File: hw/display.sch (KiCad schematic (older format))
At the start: 22 parts, among them J1 AMPSEAL_8_POS_776275-1, J101 HEADER_MOLEX_54104-4031, J4 HEADER_MOLEX_52207-0433, U1 MCP2551_SOIC8, U2 ALLIANCE_AS4C4M16SA_TSOP_II, U3 WINDBOND_W25Q32FV_SOIC8_W, U6 MOSFET-N_2N7002W, X101 XTAL_ABS25-32.768KHZ-T, X3 BUZZER_PKM13EPYH4002-B0

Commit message: still implementing treeview, not ready
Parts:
- removed U6: MOSFET-N_2N7002W, usevolt:SOT323, symbol MOSFET-N_2N7002W-RESCUE-display
- added C101: 100nF, kemet:0603, symbol 100nF
- added D101: DIODE_RS07J-GS18, usevolt:DO219AB, symbol DIODE_RS07J-GS18
- added L101: INDUCTOR_SDR1005-101KL, usevolt:INDUCTOR_BOURNS_10X13X5MM, symbol INDUCTOR_SDR1005-101KL
- added R101: R_0.33OHM, usevolt:0603, symbol R_0.33OHM
- added U101: MOSFET-N_2N7002W, usevolt:SOT323, symbol MOSFET-N_2N7002W
- added U102: AL8805W5-7_LED_DRIVER, usevolt:SOT-25, symbol AL8805W5-7_LED_DRIVER
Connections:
- wire segments 272 -> 287
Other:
- moved on the sheet: J101, X3

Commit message: hw 1.5.0 ordered
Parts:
- U1: symbol MCP2551_SOIC8 -> MCP2551_SOIC8-RESCUE-display
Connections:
- net +5V: now also U1.P$3 (VDD); no longer U1.8 (RS/GND)
- net CANH: now also U1.P$7 (CANH)
- net CANL: now also U1.P$6 (CANL)
- net GND: now also U1.P$2 (VSS), U1.P$8 (RS); no longer U1.5 (VREF)
- net lpc1785_sheet/CAN_RXD: now also U1.P$4 (RXD)
- net lpc1785_sheet/CAN_TXD: now also U1.P$1 (TXD)
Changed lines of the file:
@@
 CANL
 $Comp
-L MCP2551_SOIC8 U1
+L MCP2551_SOIC8-RESCUE-display U1
 U 1 1 57BD7966
 P 2900 3300

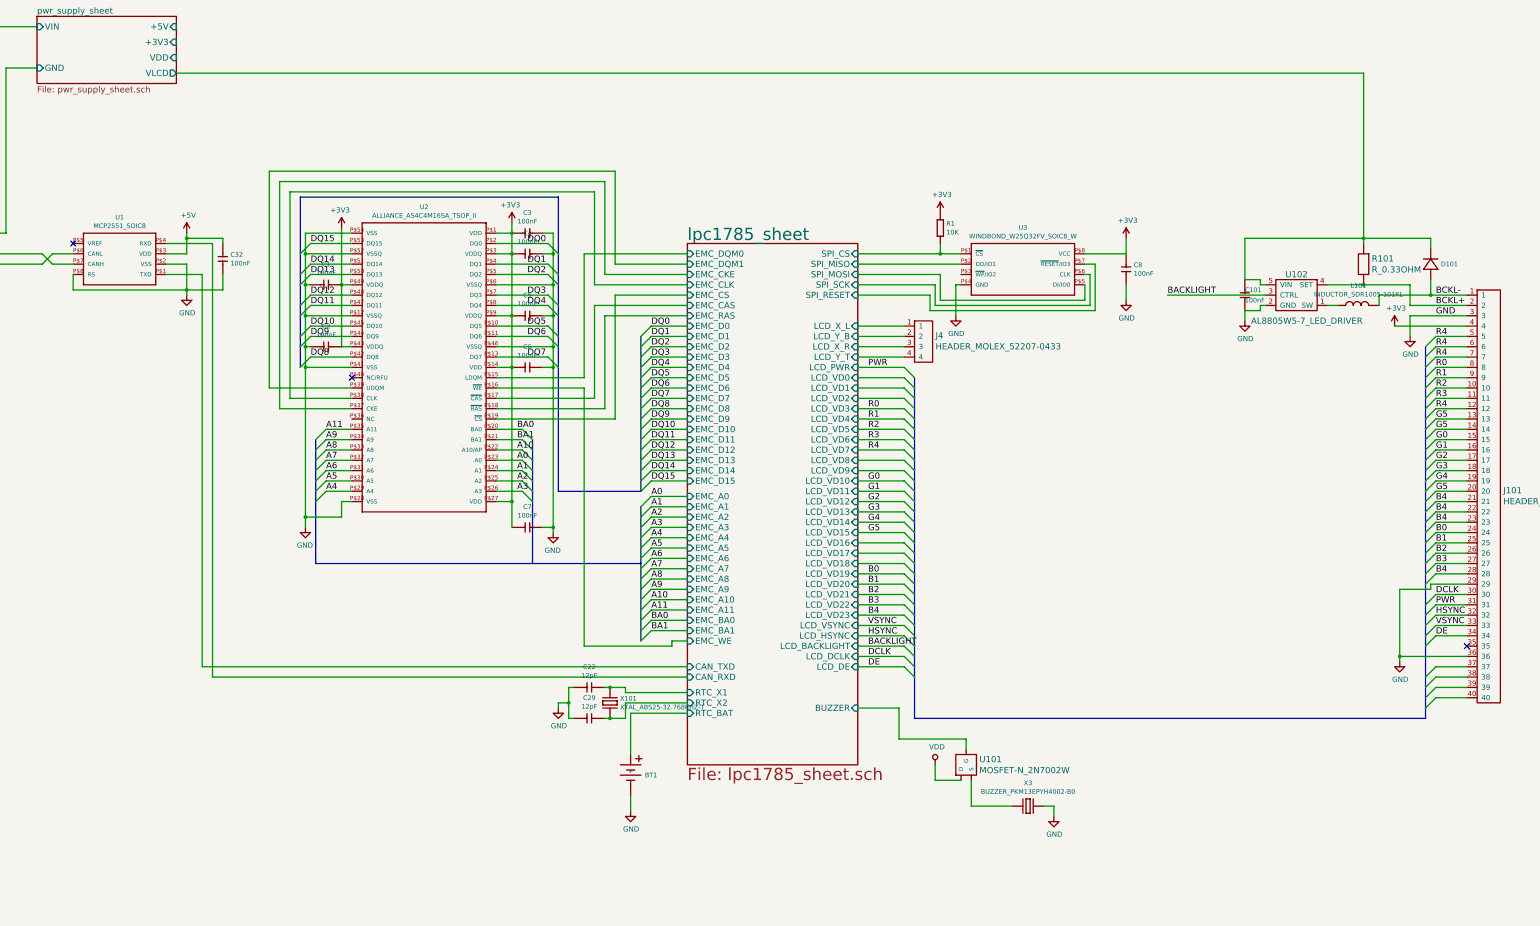
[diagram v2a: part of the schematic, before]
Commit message: hw version 1.6.0
* LCD backlight remains off while booting
* BUZZER amplifying MOSFET circuit changed to low side driving
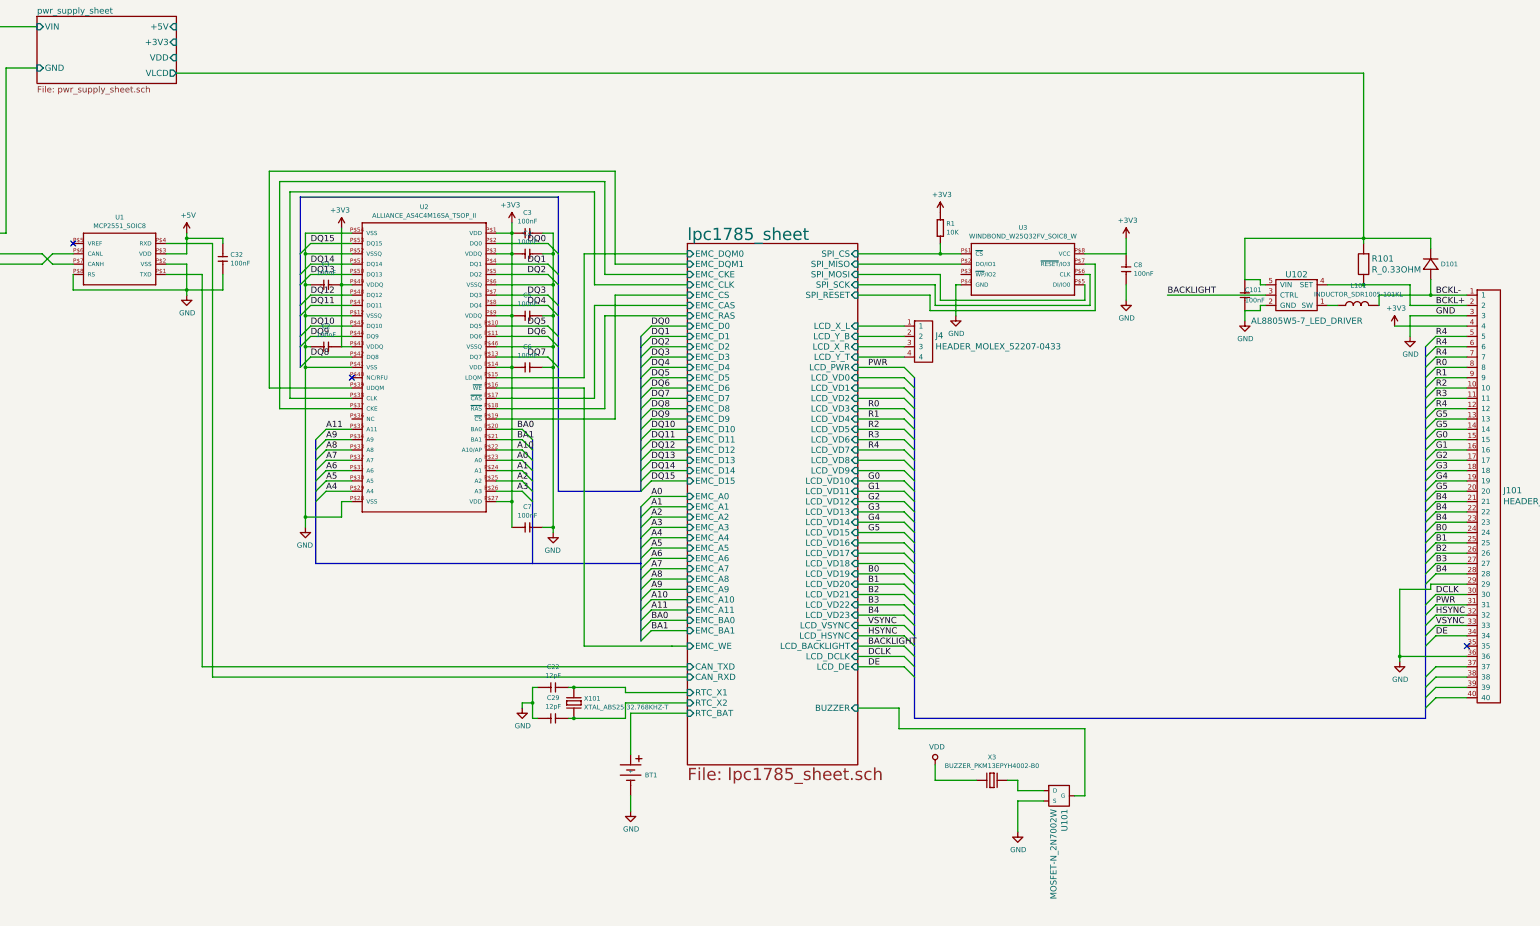
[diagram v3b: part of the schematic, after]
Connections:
- net GND: now also U101.R (S); no longer X3.2 (P$2)
- net VDD: now also X3.1 (P$1); no longer U101.M (D)
- new net: U101.M (D), X3.2 (P$2)
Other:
- moved on the sheet: C22, C29, U101, X101, X3

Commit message: implementing a multilinguality
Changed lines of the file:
@@
 	14750 3600 15600 3600
 Wire Bus Line
-	10250 7700 15200 7700
-Wire Bus Line
-	10250 4400 10250 7700
+	15200 7700 10250 7700
+Wire Bus Line
+	10250 7700 10250 4400
 Wire Wire Line
 	15300 7500 15600 7500
@@
 	7600 4000 7600 5500
 Wire Bus Line
-	6800 5500 7600 5500
-Wire Bus Line
-	6800 2650 6800 5500
+	7600 5500 6800 5500
+Wire Bus Line
+	6800 5500 6800 2650
 Wire Bus Line
 	6800 2650 4300 2650
@@
 Wire Wire Line
 	14600 1450 3100 1450
-$Comp
-L INDUCTOR_SDR1005-101KL L101
-U 1 1 58F7C6AA
-P 14550 3700
-F 0 "L101" H 14550 3891 45  0000 C CNN
-F 1 "INDUCTOR_SDR1005-101KL" H 14550 3807 45  0000 C CNN
-F 2 "usevolt:INDUCTOR_BOURNS_10X13X5MM" H 14580 3850 20  0001 C CNN
-F 3 "http://www.farnell.com/datasheets/1695384.pdf?_ga=1.223340891.1948984246.1460023966" H 14450 3640 60  0001 C CNN
-F 4 "1828057" H 14850 4040 60  0001 C CNN "1st Source Part Number"
-F 5 "BOURNS" H 14550 3740 60  0001 C CNN "Manufacturer"
-F 6 "Digi-Key" H 14950 4140 60  0001 C CNN "2nd Source"
-F 7 "Farnell" H 14750 3940 60  0001 C CNN "1st Source"
-F 8 "SDR1005-101KL" H 14650 3840 60  0001 C CNN "Manufacturer Part Number"
-F 9 "SDR1005-101KLCT-ND" H 15050 4240 60  0001 C CNN "2nd Source Part Number"
-	1    14550 3700
-	1    0    0    -1
-$EndComp
 Wire Wire Line
 	10450 8300 10850 8300
@@
 Wire Wire Line
 	10500 3650 11900 3650
+$Comp
+L INDUCTOR_SDR1005-101KL L101
+U 1 1 58F7C6AA
+P 14550 3700
+F 0 "L101" H 14550 3891 45  0000 C CNN
+F 1 "INDUCTOR_SDR1005-101KL" H 14550 3807 45  0000 C CNN
+F 2 "usevolt:INDUCTOR_BOURNS_10X13X5MM" H 14580 3850 20  0001 C CNN
+F 3 "http://www.farnell.com/datasheets/1695384.pdf?_ga=1.223340891.1948984246.1460023966" H 14450 3640 60  0001 C CNN
+F 4 "1828057" H 14850 4040 60  0001 C CNN "1st Source Part Number"
+F 5 "BOURNS" H 14550 3740 60  0001 C CNN "Manufacturer"
+F 6 "Digi-Key" H 14950 4140 60  0001 C CNN "2nd Source"
+F 7 "Farnell" H 14750 3940 60  0001 C CNN "1st Source"
+F 8 "SDR1005-101KL" H 14650 3840 60  0001 C CNN "Manufacturer Part Number"
+F 9 "SDR1005-101KLCT-ND" H 15050 4240 60  0001 C CNN "2nd Source Part Number"
+	1    14550 3700
+	1    0    0    -1
+$EndComp
 $EndSCHEMATC

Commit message: porting uv0a_hds pcb to uw_display
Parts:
- removed BT1: BATTERY_HOLDER_CH7410-2032LFSMD, usevolt:usevolt-BATTERY_HOLDER_CH7410-2032LF, symbol BATTERY_HOLDER_CH7410-2032LFSMD
- removed C1, C2, C3, C32, C4, C5, C6, C7, C8: 100nF, kemet:Kemet-CAPC1608X85N, symbol 100nF
- removed C22, C29: 12pF, kemet:Kemet-CAPC1608X85N, symbol 12pF
- removed D101: DIODE_RS07J-GS18, usevolt:DO219AB, symbol DIODE_RS07J-GS18
- removed J1: AMPSEAL_8_POS_776275-1, usevolt:AMPSEAL_8_POS_776275-1, symbol AMPSEAL_8_POS_776275-1
- removed J101: HEADER_MOLEX_54104-4031, usevolt:HEADER_MOLEX_54104-4031, symbol HEADER_MOLEX_54104-4031
- removed J4: HEADER_MOLEX_52207-0433, usevolt:HEADER_MOLEX_52207-0433, symbol HEADER_MOLEX_52207-0433
- removed L101: INDUCTOR_SDR1005-101KL, usevolt:INDUCTOR_BOURNS_10X13X5MM, symbol INDUCTOR_SDR1005-101KL
- removed R1: 10K, multicomp:Multicomp-RESC1608X60N, symbol 10K
- removed R101: R_0.33OHM, usevolt:0603, symbol R_0.33OHM
- removed U1: MCP2551_SOIC8, usevolt:SOIC8, symbol MCP2551_SOIC8-RESCUE-display
- removed U101: MOSFET-N_2N7002W, usevolt:SOT323, symbol MOSFET-N_2N7002W
- removed U102: AL8805W5-7_LED_DRIVER, usevolt:SOT-25, symbol AL8805W5-7_LED_DRIVER
- removed U2: ALLIANCE_AS4C4M16SA_TSOP_II, usevolt:TSOP_II_54_PIN, symbol ALLIANCE_AS4C4M16SA_TSOP_II
- removed U3: WINDBOND_W25Q32FV_SOIC8_W, usevolt:SOIC8_W, symbol WINDBOND_W25Q32FV_SOIC8_W
- removed X101: XTAL_ABS25-32.768KHZ-T, usevolt:XTAL_32.768KHZ-T, symbol XTAL_ABS25-32.768KHZ-T
- removed X3: BUZZER_PKM13EPYH4002-B0, usevolt:BUZZER_PKM13EPYH4002-B0, symbol BUZZER_PKM13EPYH4002-B0
- added J101: AMPSEAL_8_POS_VERT_BLACK_SEALED_1-776276-1, usevolt:AMPSEAL_8_POS_776275-1, symbol AMPSEAL_8_POS_VERT_BLACK_SEALED_1-776276-1
- added U101: MCP2551_SOIC8, usevolt:SOIC8, symbol MCP2551_SOIC8
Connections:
- net pwr_supply_sheet/VLCD is gone; now on net GND: C101.2 (C2)
- net +5V: now also C101.1 (C1), U101.3 (VDD)
- net CANH: now also J101.4 (S), U101.7 (CANH)
- net CANL: now also J101.5 (S), U101.6 (CANL)
- net GND: now also J101.2 (S), U101.2 (VSS), U101.8 (RS/GND); no longer C101.1 (C1)
- net VDD: now also J101.1 (S)
- new net lpc1549/CAN_RX: U101.4 (RXD)
- new net lpc1549/CAN_TX: U101.1 (TXD)
- no-connect marks 3 -> 0

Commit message: 1.7.0 pcb created, not yet ordered
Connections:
- net VDD: no longer J101.1 (S)
- new net power_supply/VIN: J101.1 (S)
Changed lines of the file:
@@
 F4 "+3V3" O R 3600 1600 60
 F5 "GND" I L 2400 1600 60
+F6 "VDD" I R 3600 1300 60
+F7 "VLCD" O R 3600 1200 60
 $EndSheet
 $Comp
-L GND #PWR102
+L GND #PWR01
 U 1 1 58FBFAD2
 P 1900 2050
-F 0 "#PWR102" H 1900 1800 50  0001 C CNN
+F 0 "#PWR01" H 1900 1800 50  0001 C CNN
 F 1 "GND" H 1905 1877 50  0000 C CNN
 F 2 "" H 1900 2050 50  0000 C CNN
@@
 $EndComp
 $Comp
-L GND #PWR105
+L GND #PWR02
 U 1 1 58FC1671
 P 3050 2850
-F 0 "#PWR105" H 3050 2600 50  0001 C CNN
+F 0 "#PWR02" H 3050 2600 50  0001 C CNN
 F 1 "GND" H 3055 2677 50  0000 C CNN
 F 2 "" H 3050 2850 50  0000 C CNN
@@
 $EndComp
 $Comp
-L +5V #PWR104
+L +5V #PWR03
 U 1 1 58FC16F6
 P 3050 2400
-F 0 "#PWR104" H 3050 2250 50  0001 C CNN
+F 0 "#PWR03" H 3050 2250 50  0001 C CNN
 F 1 "+5V" H 3065 2573 50  0000 C CNN
 F 2 "" H 3050 2400 50  0000 C CNN
@@
 $EndComp
 $Comp
-L +5V #PWR106
+L +5V #PWR04
 U 1 1 58FC1761
-P 3800 1400
-F 0 "#PWR106" H 3800 1250 50  0001 C CNN
-F 1 "+5V" H 3815 1573 50  0000 C CNN
-F 2 "" H 3800 1400 50  0000 C CNN
-F 3 "" H 3800 1400 50  0000 C CNN
-	1    3800 1400
-	1    0    0    -1
-$EndComp
-$Comp
-L +3V3 #PWR107
+P 4000 1400
+F 0 "#PWR04" H 4000 1250 50  0001 C CNN
+F 1 "+5V" H 4015 1573 50  0000 C CNN
+F 2 "" H 4000 1400 50  0000 C CNN
+F 3 "" H 4000 1400 50  0000 C CNN
+	1    4000 1400
+	1    0    0    -1
+$EndComp
+$Comp
+L +3V3 #PWR05
 U 1 1 58FC17CE
-P 3950 1600
-F 0 "#PWR107" H 3950 1450 50  0001 C CNN
-F 1 "+3V3" H 3965 1773 50  0000 C CNN
-F 2 "" H 3950 1600 50  0000 C CNN
-F 3 "" H 3950 1600 50  0000 C CNN
-	1    3950 1600
+P 4150 1600
+F 0 "#PWR05" H 4150 1450 50  0001 C CNN
+F 1 "+3V3" H 4165 1773 50  0000 C CNN
+F 2 "" H 4150 1600 50  0000 C CNN
+F 3 "" H 4150 1600 50  0000 C CNN
+	1    4150 1600
 	1    0    0    -1
 $EndComp
@@
 F7 "LCD_PD" O R 6400 3800 60
 F8 "LCD_CS" O R 6400 3700 60
-F12 "FLASH_CS" O R 6400 3200 60
-F13 "FLASH_MISO" I R 6400 2900 60
-F14 "FLASH_MOSI" O R 6400 3000 60
-F15 "FLASH_CLK" O R 6400 3100 60
+F9 "FLASH_CS" O R 6400 3200 60
+F10 "FLASH_MISO" I R 6400 2900 60
+F11 "FLASH_MOSI" O R 6400 3000 60
+F12 "FLASH_CLK" O R 6400 3100 60
 $EndSheet
 Wire Wire Line
@@
 	3050 2400 3050 2500
 Wire Wire Line
-	3600 1400 3800 1400
-Wire Wire Line
-	3950 1600 3600 1600
+	3600 1400 4000 1400
+Wire Wire Line
+	4150 1600 3600 1600
 Wire Wire Line
 	3050 2500 2950 2500
@@
 Wire Wire Line
 	8050 3800 6400 3800
-$Comp
-L VDD #PWR101
-U 1 1 5901EBE1
-P 1750 1100
-F 0 "#PWR101" H 1750 950 50  0001 C CNN
-F 1 "VDD" H 1767 1273 50  0000 C CNN
-F 2 "" H 1750 1100 50  0000 C CNN
-F 3 "" H 1750 1100 50  0000 C CNN
-	1    1750 1100
-	1    0    0    -1
-$EndComp
-Wire Wire Line
-	1050 1900 1750 1900
-Wire Wire Line
-	1750 1900 1750 1100
+Wire Wire Line
+	1750 1900 1050 1900
 Wire Wire Line
 	2400 1200 1750 1200
-Connection ~ 1750 1200
 $Sheet
 S 8050 2400 1050 500
@@
 	-1   0    0    -1
 $EndComp
+$Comp
+L VDD #PWR06
+U 1 1 5A0D6E53
+P 3900 1200
+F 0 "#PWR06" H 3900 1050 50  0001 C CNN
+F 1 "VDD" H 3917 1373 50  0000 C CNN
+F 2 "" H 3900 1200 50  0000 C CNN
+F 3 "" H 3900 1200 50  0000 C CNN
+	1    3900 1200
+	1    0    0    -1
+$EndComp
+Wire Wire Line
+	3900 1200 3900 1300
+Wire Wire Line
+	3900 1300 3600 1300
+$Comp
+L VEE #PWR07
+U 1 1 5A0D70BB
+P 3750 1000
+F 0 "#PWR07" H 3750 850 50  0001 C CNN
+F 1 "VEE" H 3767 1173 50  0000 C CNN
+F 2 "" H 3750 1000 50  0000 C CNN
+F 3 "" H 3750 1000 50  0000 C CNN
+	1    3750 1000
+	1    0    0    -1
+$EndComp
+Wire Wire Line
+	3750 1000 3750 1200
+Wire Wire Line
+	3750 1200 3600 1200
+Wire Wire Line
+	1750 1200 1750 1900
 $EndSCHEMATC

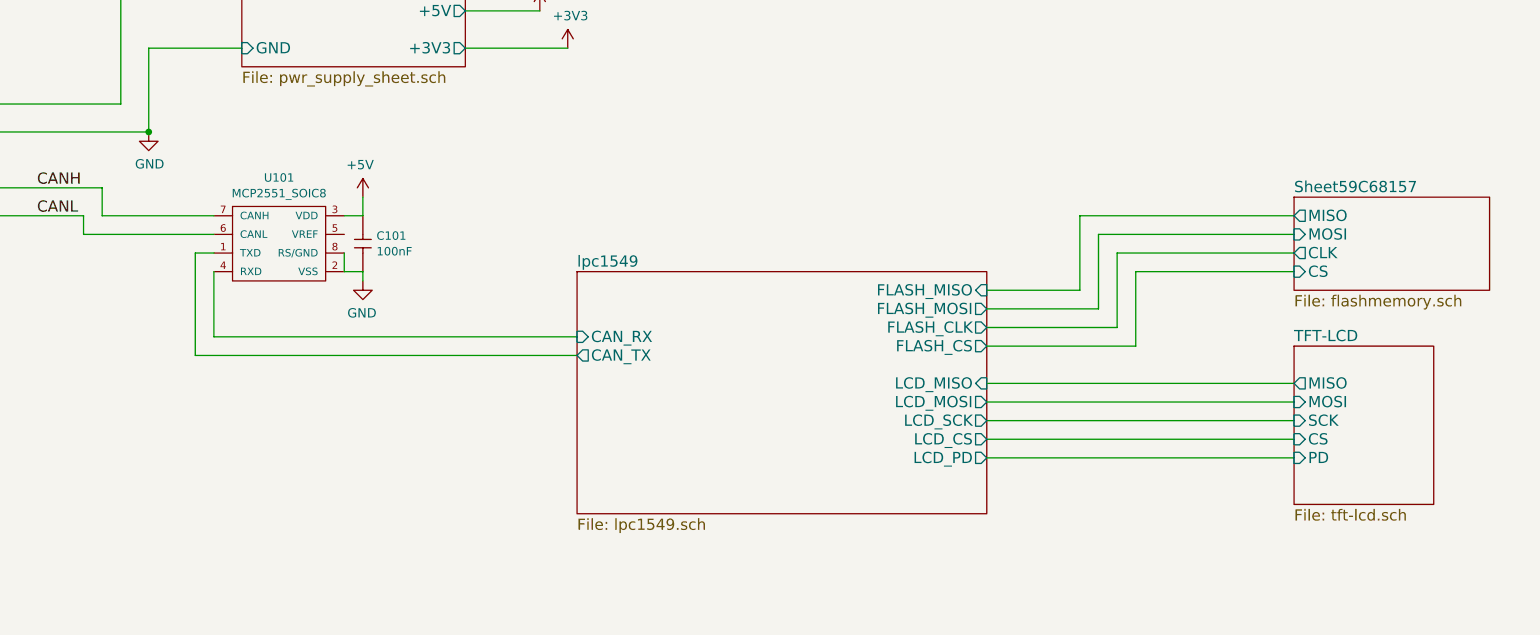
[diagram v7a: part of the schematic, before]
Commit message: uw180s grab times adjustable
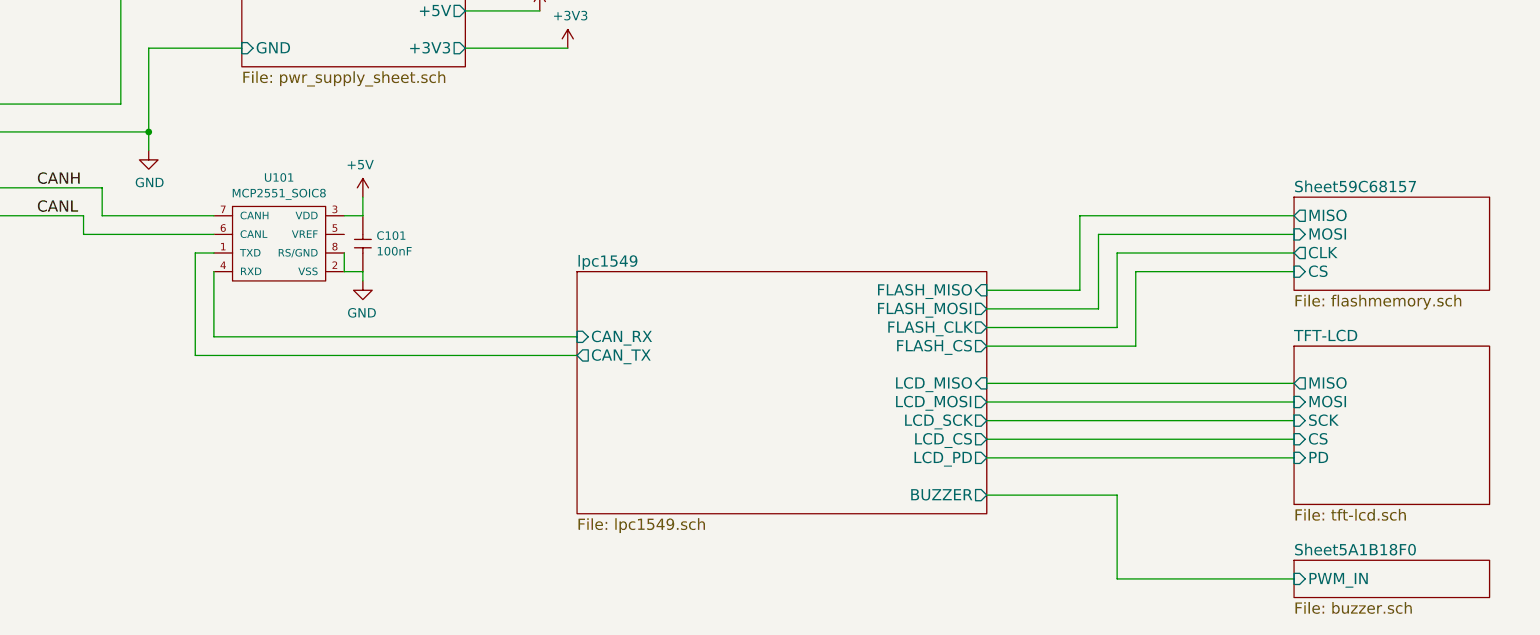
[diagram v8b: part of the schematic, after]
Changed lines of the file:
@@
 $Descr A4 11693 8268
 encoding utf-8
-Sheet 1 5
+Sheet 1 6
 Title "UV0A_hds"
 Date "2017-04-22"
@@
 L GND #PWR01
 U 1 1 58FBFAD2
-P 1900 2050
-F 0 "#PWR01" H 1900 1800 50  0001 C CNN
-F 1 "GND" H 1905 1877 50  0000 C CNN
-F 2 "" H 1900 2050 50  0000 C CNN
-F 3 "" H 1900 2050 50  0000 C CNN
-	1    1900 2050
+P 1900 2150
+F 0 "#PWR01" H 1900 1900 50  0001 C CNN
+F 1 "GND" H 1905 1977 50  0000 C CNN
+F 2 "" H 1900 2150 50  0000 C CNN
+F 3 "" H 1900 2150 50  0000 C CNN
+	1    1900 2150
 	1    0    0    -1
 $EndComp
@@
 CANL
 $Sheet
-S 8050 3200 750  850
+S 8050 3200 1050 850
 U 58FC4AA8
 F0 "TFT-LCD" 60
@@
 F11 "FLASH_MOSI" O R 6400 3000 60
 F12 "FLASH_CLK" O R 6400 3100 60
+F13 "BUZZER" O R 6400 4000 60
 $EndSheet
 Wire Wire Line
-	1050 2050 1900 2050
+	1900 2150 1900 2050
 Wire Wire Line
 	1900 2050 1900 1600
 Wire Wire Line
 	1900 1600 2400 1600
-Connection ~ 1900 2050
 Wire Wire Line
 	2950 2700 2950 2800
@@
 Wire Wire Line
 	1750 1200 1750 1900
+$Sheet
+S 8050 4350 1050 200
+U 5A1B18F1
+F0 "Sheet5A1B18F0" 60
+F1 "buzzer.sch" 60
+F2 "PWM_IN" I L 8050 4450 60
+$EndSheet
+Wire Wire Line
+	6400 4000 7100 4000
+Wire Wire Line
+	7100 4000 7100 4450
+Wire Wire Line
+	7100 4450 8050 4450
+Wire Wire Line
+	1050 2050 1900 2050
+Connection ~ 1900 2050
 $EndSCHEMATC
